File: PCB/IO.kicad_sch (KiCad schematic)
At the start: 39 parts, among them J401 Conn_01x05_Pin, J402 USB_C_Receptacle_USB2.0_16P, J403 Screw_Terminal_01x06, J404 Screw_Terminal_01x04, J405 Conn_02x03_Counter_Clockwise, J406 Conn_02x03_Counter_Clockwise, J408 Conn_01x04, Q401 SL2302S, SW401 SW_Push, SW402 SW_Push

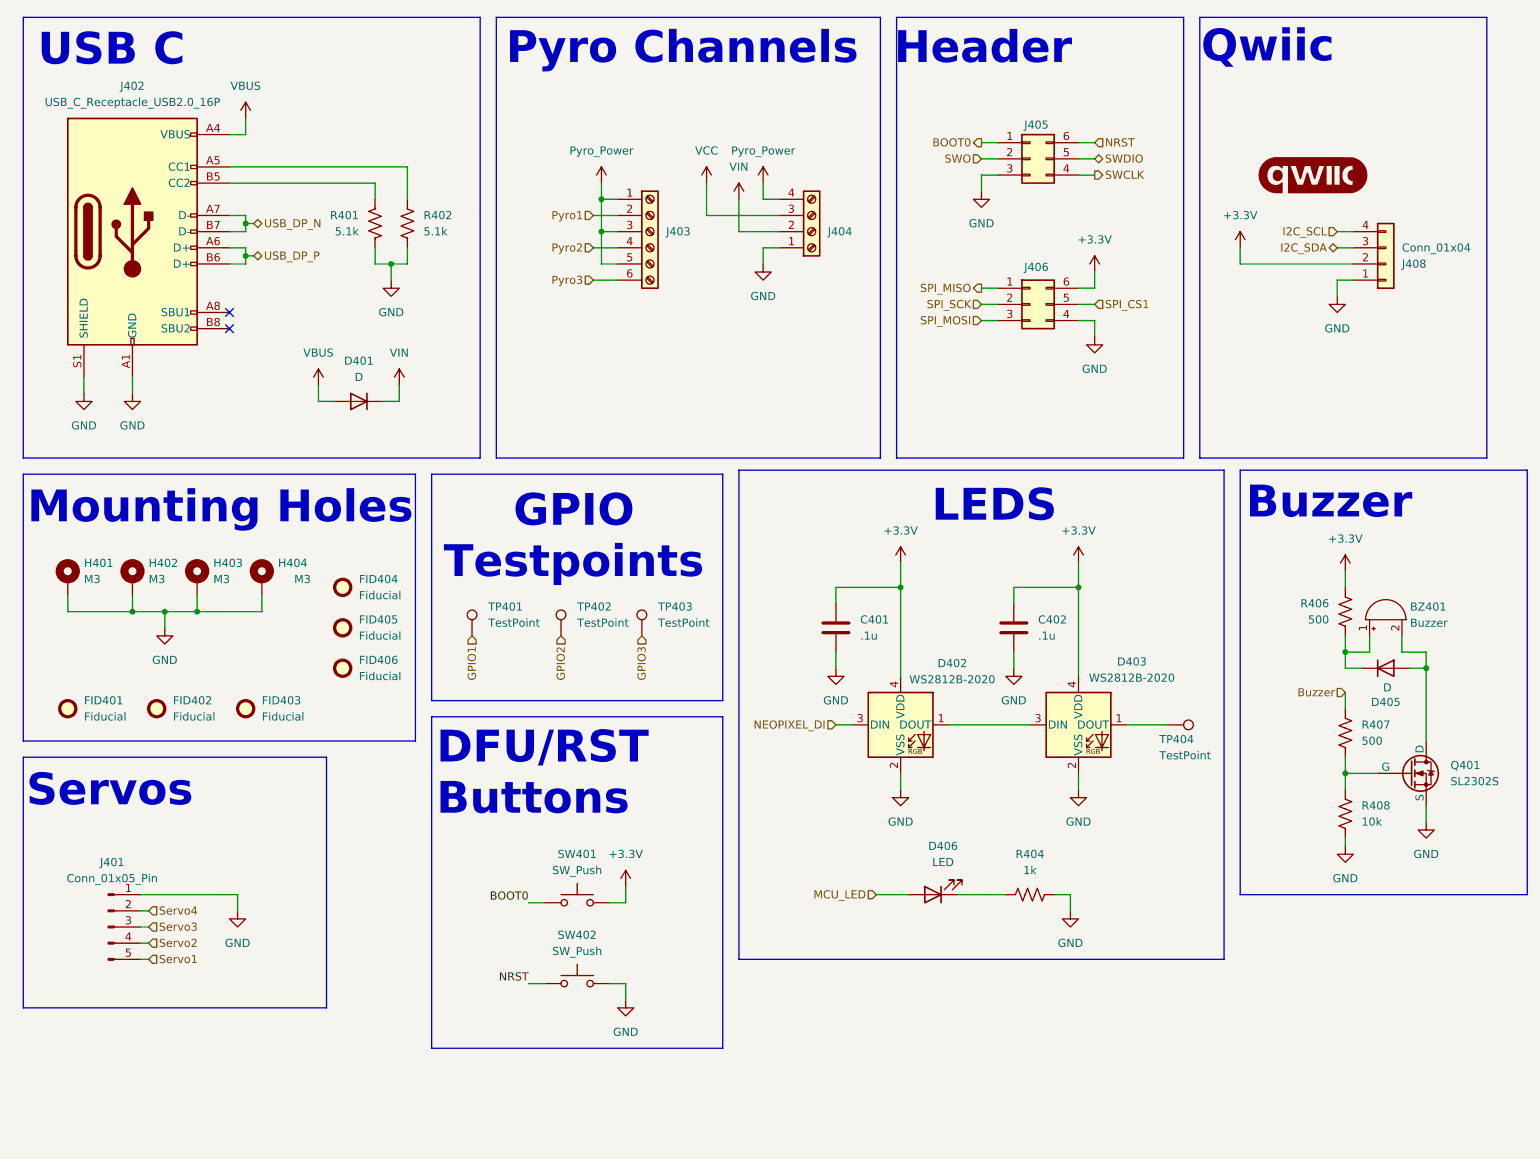
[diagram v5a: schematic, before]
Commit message: - Renamed all NETs connected to MCU sheet to the pin name - Cleaned up schematic - Named all unnamed NETs
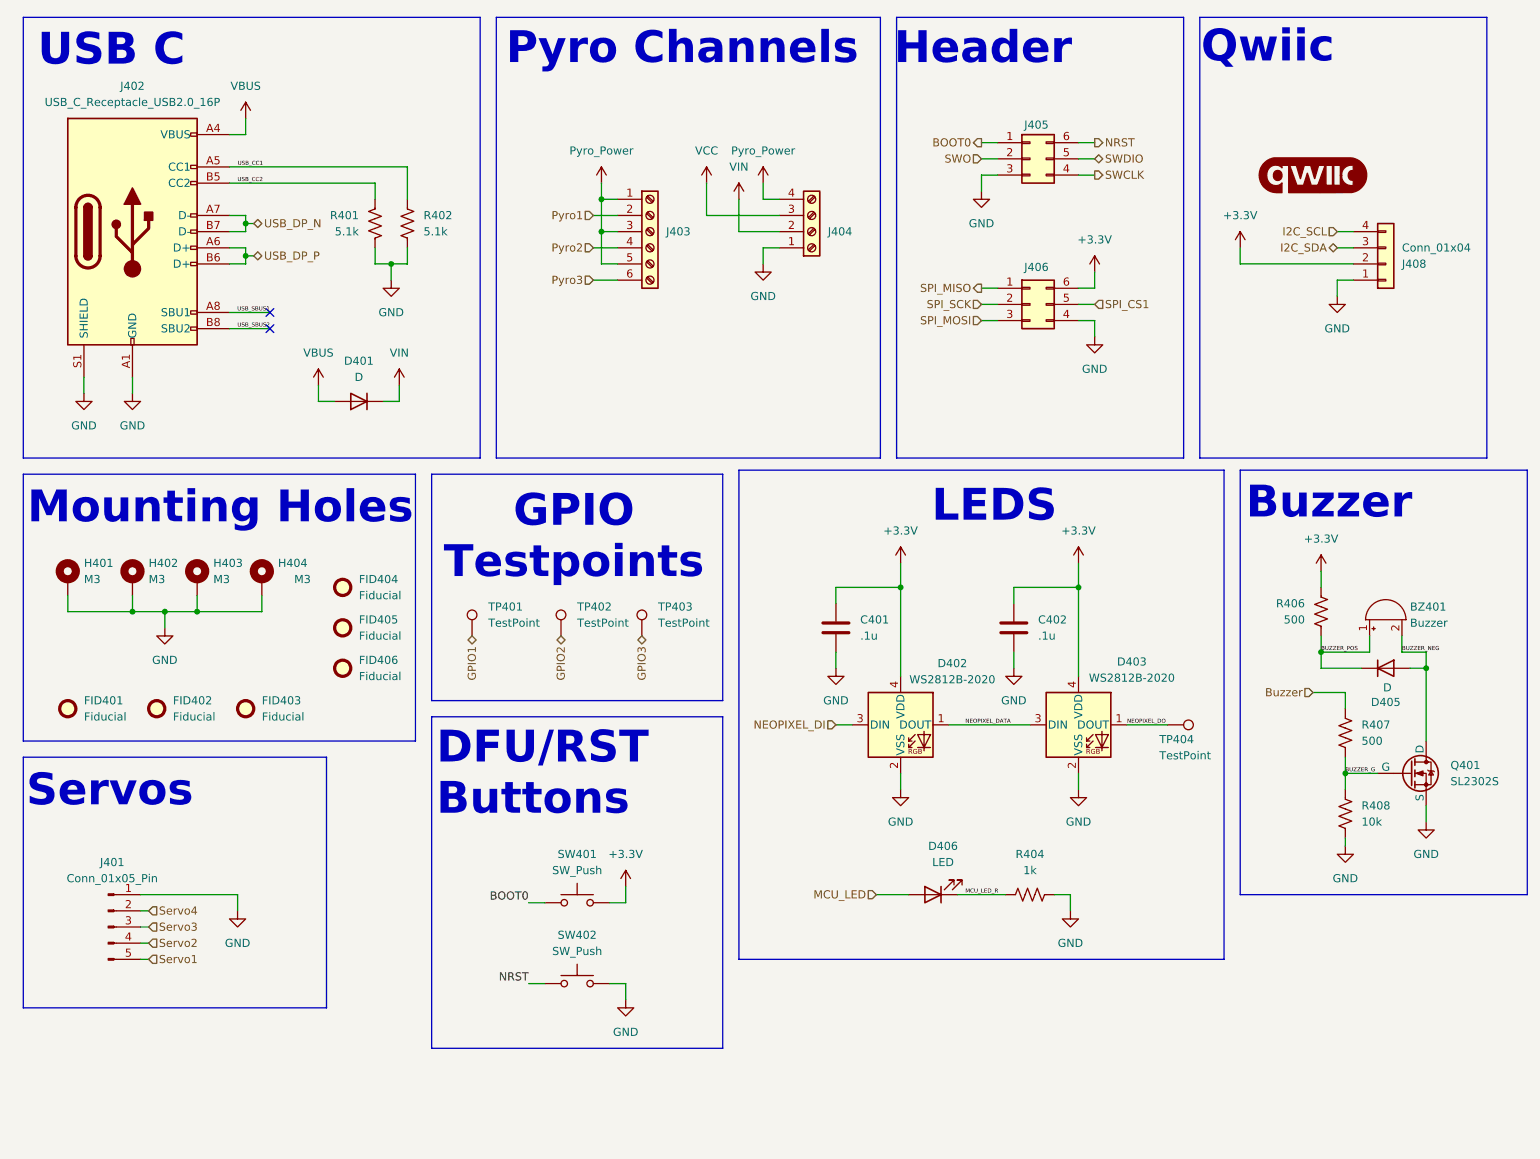
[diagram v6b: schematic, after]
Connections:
- net BUZZER_POS: now reaches BZ401.1 (+), D405.1 (K), R406.2
- net BUZZER_NEG: now reaches BZ401.2 (-), D405.2 (A), Q401.3 (D)
- net BUZZER_G: now reaches Q401.1 (G), R407.2, R408.1
- net MCU_LED_R: now reaches D406.1 (K), R404.1
- net NEOPIXEL_DATA: now reaches D402.1 (DOUT), D403.3 (DIN)
- net USB_CC1: now reaches J402.A5 (CC1), R402.1
- net USB_SBUS1: now reaches J402.A8 (SBU1)
- net USB_CC2: now reaches J402.B5 (CC2), R401.1
- net USB_SBUS2: now reaches J402.B8 (SBU2)
- net NEOPIXEL_DO: now reaches D403.1 (DOUT), TP404.1
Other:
- moved on the sheet: R406
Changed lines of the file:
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@@
 	)
 	(junction
-		(at 222.25 114.3)
+		(at 218.44 114.3)
 		(diameter 0)
 		(color 0 0 0 0)
@@
 	)
 	(no_connect
-		(at 46.99 60.96)
+		(at 53.34 60.96)
 	)
 	(no_connect
-		(at 46.99 63.5)
+		(at 53.34 63.5)
 	)
 	(wire
@@
 	(wire
 		(pts
-			(xy 161.29 152.4) (xy 168.91 152.4)
+			(xy 180.34 133.35) (xy 180.34 135.89)
 		)
 		(stroke
@@
 	(wire
 		(pts
-			(xy 180.34 133.35) (xy 180.34 135.89)
+			(xy 31.75 73.66) (xy 31.75 71.12)
 		)
 		(stroke
@@
 	(wire
 		(pts
-			(xy 31.75 73.66) (xy 31.75 71.12)
+			(xy 46.99 63.5) (xy 53.34 63.5)
 		)
 		(stroke
@@
 	(wire
 		(pts
+			(xy 226.06 114.3) (xy 226.06 111.76)
+		)
+		(stroke
+			(width 0)
+			(type default)
+		)
+	)
+	(wire
+		(pts
 			(xy 182.88 36.83) (xy 180.34 36.83)
 		)
@@
 	(wire
 		(pts
-			(xy 222.25 120.65) (xy 222.25 123.19)
-		)
-		(stroke
-			(width 0)
-			(type default)
-		)
-	)
-	(wire
-		(pts
 			(xy 205.74 50.8) (xy 205.74 53.34)
 		)
@@
 	(wire
 		(pts
-			(xy 226.06 111.76) (xy 226.06 114.3)
+			(xy 107.95 53.34) (xy 105.41 53.34)
 		)
 		(stroke
@@
 	(wire
 		(pts
-			(xy 107.95 53.34) (xy 105.41 53.34)
+			(xy 218.44 114.3) (xy 218.44 116.84)
 		)
 		(stroke
@@
 	(wire
 		(pts
-			(xy 222.25 114.3) (xy 222.25 116.84)
+			(xy 217.17 120.65) (xy 222.25 120.65)
 		)
 		(stroke
@@
 	(wire
 		(pts
-			(xy 222.25 114.3) (xy 226.06 114.3)
+			(xy 218.44 114.3) (xy 226.06 114.3)
 		)
 		(stroke
@@
 	(wire
 		(pts
+			(xy 161.29 152.4) (xy 168.91 152.4)
+		)
+		(stroke
+			(width 0)
+			(type default)
+		)
+	)
+	(wire
+		(pts
 			(xy 182.88 57.15) (xy 180.34 57.15)
 		)
@@
 	(wire
 		(pts
-			(xy 222.25 101.6) (xy 222.25 104.14)
+			(xy 218.44 101.6) (xy 218.44 104.14)
 		)
 		(stroke
@@
 	(wire
 		(pts
+			(xy 46.99 60.96) (xy 53.34 60.96)
+		)
+		(stroke
+			(width 0)
+			(type default)
+		)
+	)
+	(wire
+		(pts
 			(xy 142.24 114.3) (xy 142.24 116.84)
 		)
@@
 	(wire
 		(pts
+			(xy 222.25 120.65) (xy 222.25 123.19)
+		)
+		(stroke
+			(width 0)
+			(type default)
+		)
+	)
+	(wire
+		(pts
 			(xy 142.24 125.73) (xy 144.78 125.73)
 		)
@@
 	(wire
 		(pts
-			(xy 222.25 114.3) (xy 222.25 111.76)
+			(xy 218.44 114.3) (xy 218.44 111.76)
 		)
 		(stroke
@@
 	(wire
 		(pts
-			(xy 222.25 116.84) (xy 224.79 116.84)
+			(xy 218.44 116.84) (xy 224.79 116.84)
 		)
 		(stroke
@@
 		)
 	)
+	(label "USB_SBUS2"
+		(at 53.34 63.5 180)
+		(effects
+			(font
+				(size 0.635 0.635)
+			)
+			(justify right bottom)
+		)
+	)
+	(label "USB_CC2"
+		(at 48.2406 40.64 0)
+		(effects
+			(font
+				(size 0.635 0.635)
+			)
+			(justify left bottom)
+		)
+	)
 	(label "NRST"
 		(at 93.98 166.37 180)
@@
 		)
 	)
+	(label "BUZZER_POS"
+		(at 218.44 114.3 0)
+		(effects
+			(font
+				(size 0.635 0.635)
+			)
+			(justify left bottom)
+		)
+	)
+	(label "BUZZER_G"
+		(at 222.25 133.35 0)
+		(effects
+			(font
+				(size 0.635 0.635)
+			)
+			(justify left bottom)
+		)
+	)
+	(label "USB_CC1"
+		(at 48.26 38.1 0)
+		(effects
+			(font
+				(size 0.635 0.635)
+			)
+			(justify left bottom)
+		)
+	)
+	(label "MCU_LED_R"
+		(at 162.56 152.4 0)
+		(effects
+			(font
+				(size 0.635 0.635)
+			)
+			(justify left bottom)
+		)
+	)
+	(label "NEOPIXEL_DATA"
+		(at 162.56 125.73 0)
+		(effects
+			(font
+				(size 0.635 0.635)
+			)
+			(justify left bottom)
+		)
+	)
+	(label "BUZZER_NEG"
+		(at 231.14 114.3 0)
+		(effects
+			(font
+				(size 0.635 0.635)
+			)
+			(justify left bottom)
+		)
+	)
+	(label "USB_SBUS1"
+		(at 53.3206 60.96 180)
+		(effects
+			(font
+				(size 0.635 0.635)
+			)
+			(justify right bottom)
+		)
+	)
+	(label "NEOPIXEL_DO"
+		(at 187.96 125.73 0)
+		(effects
+			(font
+				(size 0.635 0.635)
+			)
+			(justify left bottom)
+		)
+	)
 	(label "BOOT0"
 		(at 93.98 153.67 180)
@@
 	)
 	(hierarchical_label "GPIO2"
-		(shape input)
+		(shape bidirectional)
 		(at 99.06 111.76 270)
 		(effects
@@
 	)
 	(hierarchical_label "GPIO1"
-		(shape input)
+		(shape bidirectional)
 		(at 85.09 111.76 270)
 		(effects
@@
 	)
 	(hierarchical_label "NRST"
-		(shape input)
+		(shape output)
 		(at 182.88 34.29 0)
 		(effects
@@
 	(hierarchical_label "Buzzer"
 		(shape input)
-		(at 222.25 120.65 180)
+		(at 217.17 120.65 180)
 		(effects
 			(font
@@
 	)
 	(hierarchical_label "GPIO3"
-		(shape input)
+		(shape bidirectional)
 		(at 111.76 111.76 270)
 		(effects
@@
 	(symbol
 		(lib_id "Device:R_US")
-		(at 222.25 107.95 0)
+		(at 218.44 107.95 0)
 		(unit 1)
 		(body_style 1)
@@
 		(dnp no)
 		(property "Reference" "R406"
-			(at 219.71 106.6799 0)
+			(at 215.9 106.6799 0)
 			(show_name no)
 			(do_not_autoplace no)
@@
 		)
 		(property "Value" "500"
-			(at 219.71 109.2199 0)
+			(at 215.9 109.2199 0)
 			(show_name no)
 			(do_not_autoplace no)
@@
 		)
 		(property "Footprint" "Resistor_SMD:R_0603_1608Metric_Pad0.98x0.95mm_HandSolder"
-			(at 223.266 108.204 90)
+			(at 219.456 108.204 90)
 			(hide yes)
 			(show_name no)
@@
 		)
 		(property "Datasheet" ""
-			(at 222.25 107.95 0)
+			(at 218.44 107.95 0)
 			(hide yes)
 			(show_name no)
@@
 		)
 		(property "Description" "Resistor, US symbol"
-			(at 222.25 107.95 0)
+			(at 218.44 107.95 0)
 			(hide yes)
 			(show_name no)
@@
 	(symbol
 		(lib_id "power:+3.3V")
-		(at 222.25 101.6 0)
+		(at 218.44 101.6 0)
 		(mirror y)
 		(unit 1)
@@
 		(fields_autoplaced yes)
 		(property "Reference" "#PWR0424"
-			(at 222.25 105.41 0)
+			(at 218.44 105.41 0)
 			(hide yes)
 			(show_name no)
@@
 		)
 		(property "Value" "+3.3V"
-			(at 222.25 96.52 0)
+			(at 218.44 96.52 0)
 			(show_name no)
 			(do_not_autoplace no)
@@
 		)
 		(property "Footprint" ""
-			(at 222.25 101.6 0)
+			(at 218.44 101.6 0)
 			(hide yes)
 			(show_name no)
@@
 		)
 		(property "Datasheet" ""
-			(at 222.25 101.6 0)
+			(at 218.44 101.6 0)
 			(hide yes)
 			(show_name no)
@@
 		)
 		(property "Description" "Power symbol creates a global label with name \"+3.3V\""
-			(at 222.25 101.6 0)
+			(at 218.44 101.6 0)
 			(hide yes)
 			(show_name no)
